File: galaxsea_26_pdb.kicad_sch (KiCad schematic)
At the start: 0 parts

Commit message: Fix annotations
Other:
- sheet 5V BDC renamed BDC Module
- removed sheet 12V BDC
- sheet BDC Module: file 5V_BDC_Module.kicad_sch -> BDC_Module.kicad_sch
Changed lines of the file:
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@@
 	(paper "A4")
 	(sheet
-		(at 174.625 53.34)
+		(at 198.755 33.655)
 		(size 53.975 34.925)
 		(exclude_from_sim no)
@@
 			(color 0 0 0 0.0000)
 		)
-		(property "Sheetname" "5V BDC"
-			(at 174.625 52.6284 0)
+		(property "Sheetname" "BDC Module"
+			(at 198.755 32.9434 0)
 			(effects
 				(font
@@
 			)
 		)
-		(property "Sheetfile" "5V_BDC_Module.kicad_sch"
-			(at 174.625 88.8496 0)
+		(property "Sheetfile" "BDC_Module.kicad_sch"
+			(at 198.755 69.1646 0)
 			(effects
 				(font
@@
 				)
 			)
-		)
-	)
-	(sheet
-		(at 175.26 99.06)
-		(size 53.975 34.925)
-		(exclude_from_sim no)
-		(in_bom yes)
-		(on_board yes)
-		(dnp no)
-		(fields_autoplaced yes)
-		(stroke
-			(width 0.1524)
-			(type solid)
-		)
-		(fill
-			(color 0 0 0 0.0000)
-		)
-		(property "Sheetname" "12V BDC"
-			(at 175.26 98.3484 0)
-			(effects
-				(font
-					(size 1.27 1.27)
-				)
-				(justify left bottom)
-			)
-		)
-		(property "Sheetfile" "12V_BDC_Module.kicad_sch"
-			(at 175.26 134.5696 0)
-			(effects
-				(font
-					(size 1.27 1.27)
-				)
-				(justify left top)
-			)
-		)
-		(instances
-			(project "galaxsea_26_pdb"
-				(path "/62a79688-1caa-411a-b477-96e92006e83c"
-					(page "3")
-				)
-			)

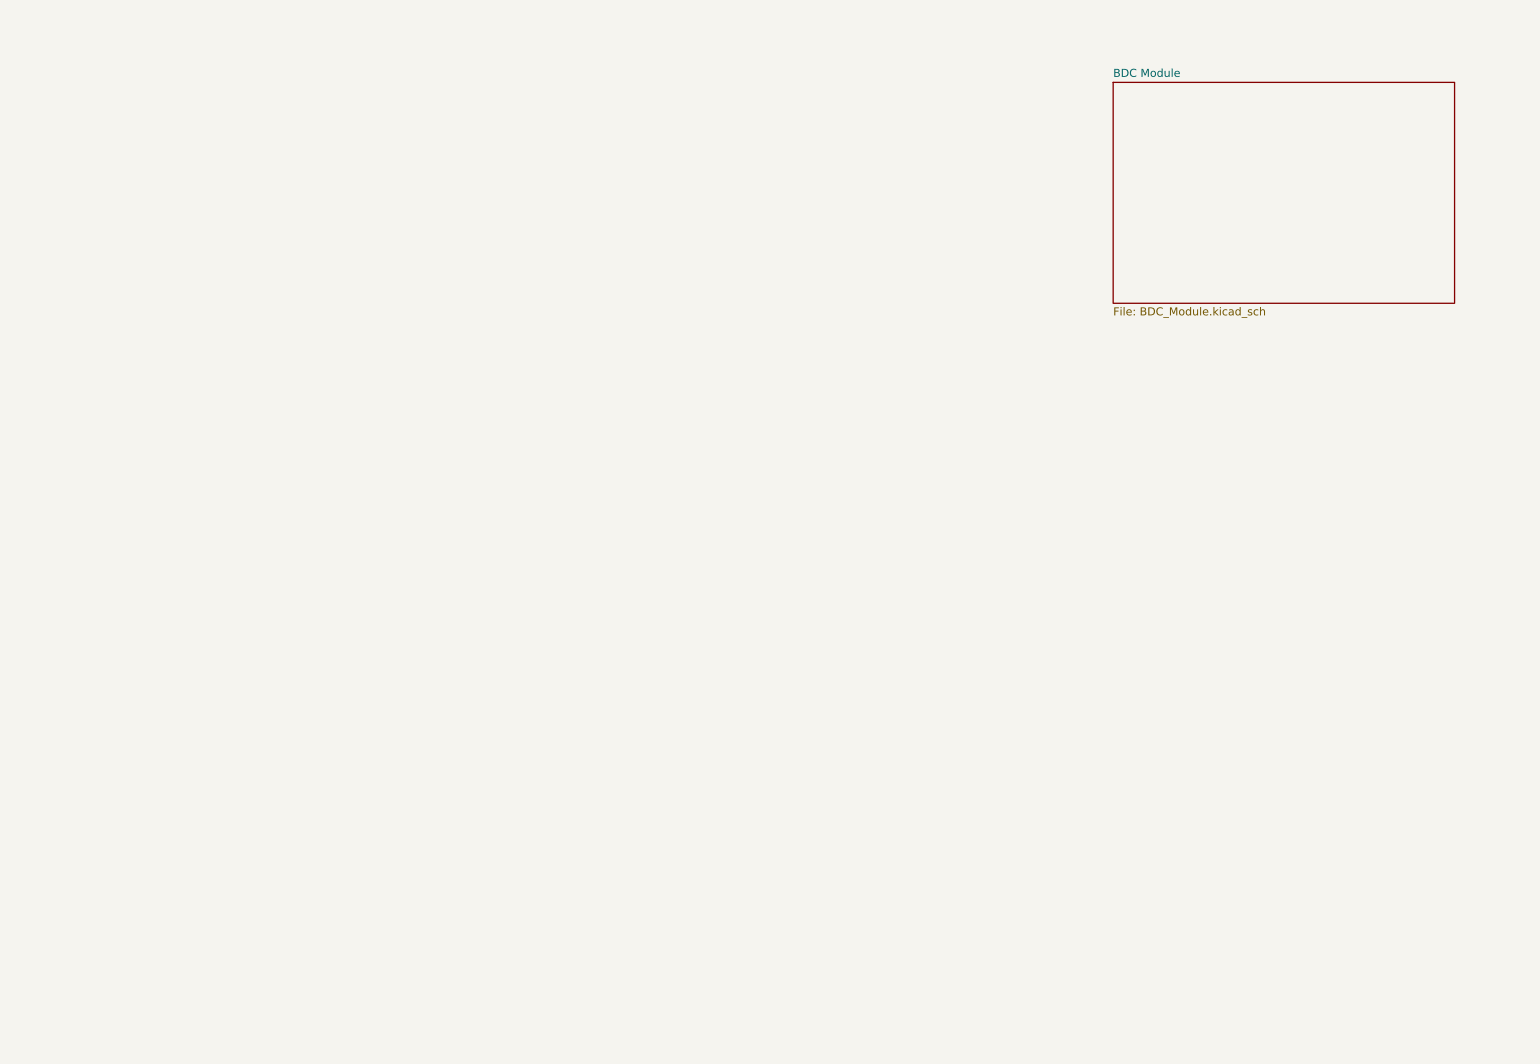
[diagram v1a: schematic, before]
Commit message: add JLCPCB design rules
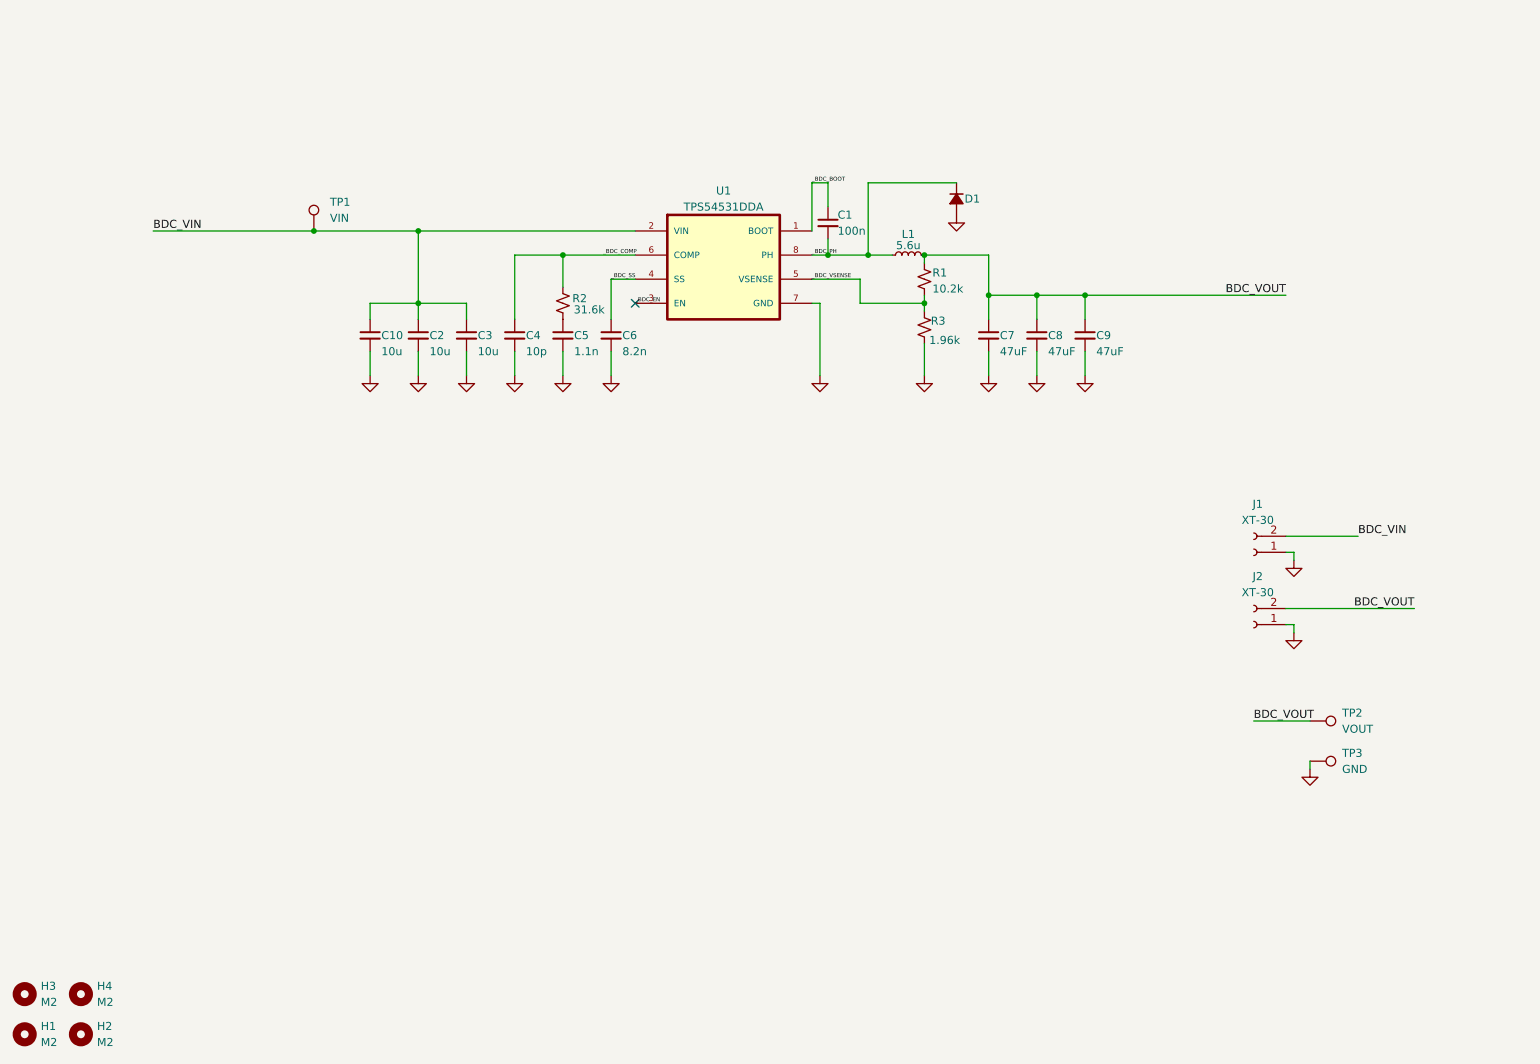
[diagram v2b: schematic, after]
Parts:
- added C1: 100n, Capacitor_SMD:C_0805_2012Metric, symbol Device:C_Small
- added C10, C2, C3: 10u, Capacitor_SMD:C_0805_2012Metric, symbol Device:C_Small
- added C4: 10p, Capacitor_SMD:C_0805_2012Metric, symbol Device:C_Small
- added C5: 1.1n, Capacitor_SMD:C_0805_2012Metric, symbol Device:C_Small
- added C6: 8.2n, Capacitor_SMD:C_0805_2012Metric, symbol Device:C_Small
- added C7, C8, C9: 47uF, Capacitor_SMD:C_0805_2012Metric, symbol Device:C_Small
- added D1: CHANGE FOOTPRINT LATER, Diode_SMD:D_SMC, symbol Device:D_Small_Filled
- added H1, H2, H3, H4: M2, MountingHole:MountingHole_2.2mm_M2, symbol Mechanical:MountingHole
- added J1, J2: XT-30, Connector_AMASS:AMASS_XT60-F_1x02_P7.20mm_Vertical, symbol Connector:Conn_01x02_Socket
- added L1: 5.6u, Inductor_SMD:L_Vishay_IHLP-2525, symbol Device:L_Small
- added R1: 10.2k, Resistor_SMD:R_0805_2012Metric, symbol Device:R_Small_US
- added R2: 31.6k, Resistor_SMD:R_0805_2012Metric, symbol Device:R_Small_US
- added R3: 1.96k, Resistor_SMD:R_0805_2012Metric, symbol Device:R_Small_US
- added TP1: VIN, TestPoint:TestPoint_Keystone_5005-5009_Compact, symbol Connector:TestPoint
- added TP2: VOUT, TestPoint:TestPoint_Keystone_5005-5009_Compact, symbol Connector:TestPoint
- added TP3: GND, TestPoint:TestPoint_Keystone_5005-5009_Compact, symbol Connector:TestPoint
- added U1: TPS54531DDA, footprints:VREG_LM5017MR_NOPB, symbol TPS54531DDA:TPS54531DDA
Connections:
- new net: C5.1, R2.1
- new net BDC_VIN: C10.1, C2.1, C3.1, J1.2 (Pin_2), TP1.1, U1.2 (VIN)
- new net BDC_VOUT: C7.1, C8.1, C9.1, J2.2 (Pin_2), L1.2, R1.1, TP2.1
- new net GND: C10.2, C2.2, C3.2, C4.2, C5.2, C6.2, C7.2, C8.2, C9.2, D1.2 (A), J1.1 (Pin_1), J2.1 (Pin_1), R3.2, TP3.1, U1.7 (GND)
- new net _BDC_BOOT: C1.1, U1.1 (BOOT)
- new net _BDC_COMP: C4.1, R2.2, U1.6 (COMP)
- new net _BDC_EN: U1.3 (EN)
- new net _BDC_PH: C1.2, D1.1 (K), L1.1, U1.8 (PH)
- new net _BDC_SS: C6.1, U1.4 (SS)
- new net _BDC_VSENSE: R1.2, R3.1, U1.5 (VSENSE)
- no-connect marks 0 -> 1
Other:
- removed sheet BDC Module

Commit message: move test and production modules into seperate hierarchical sheets
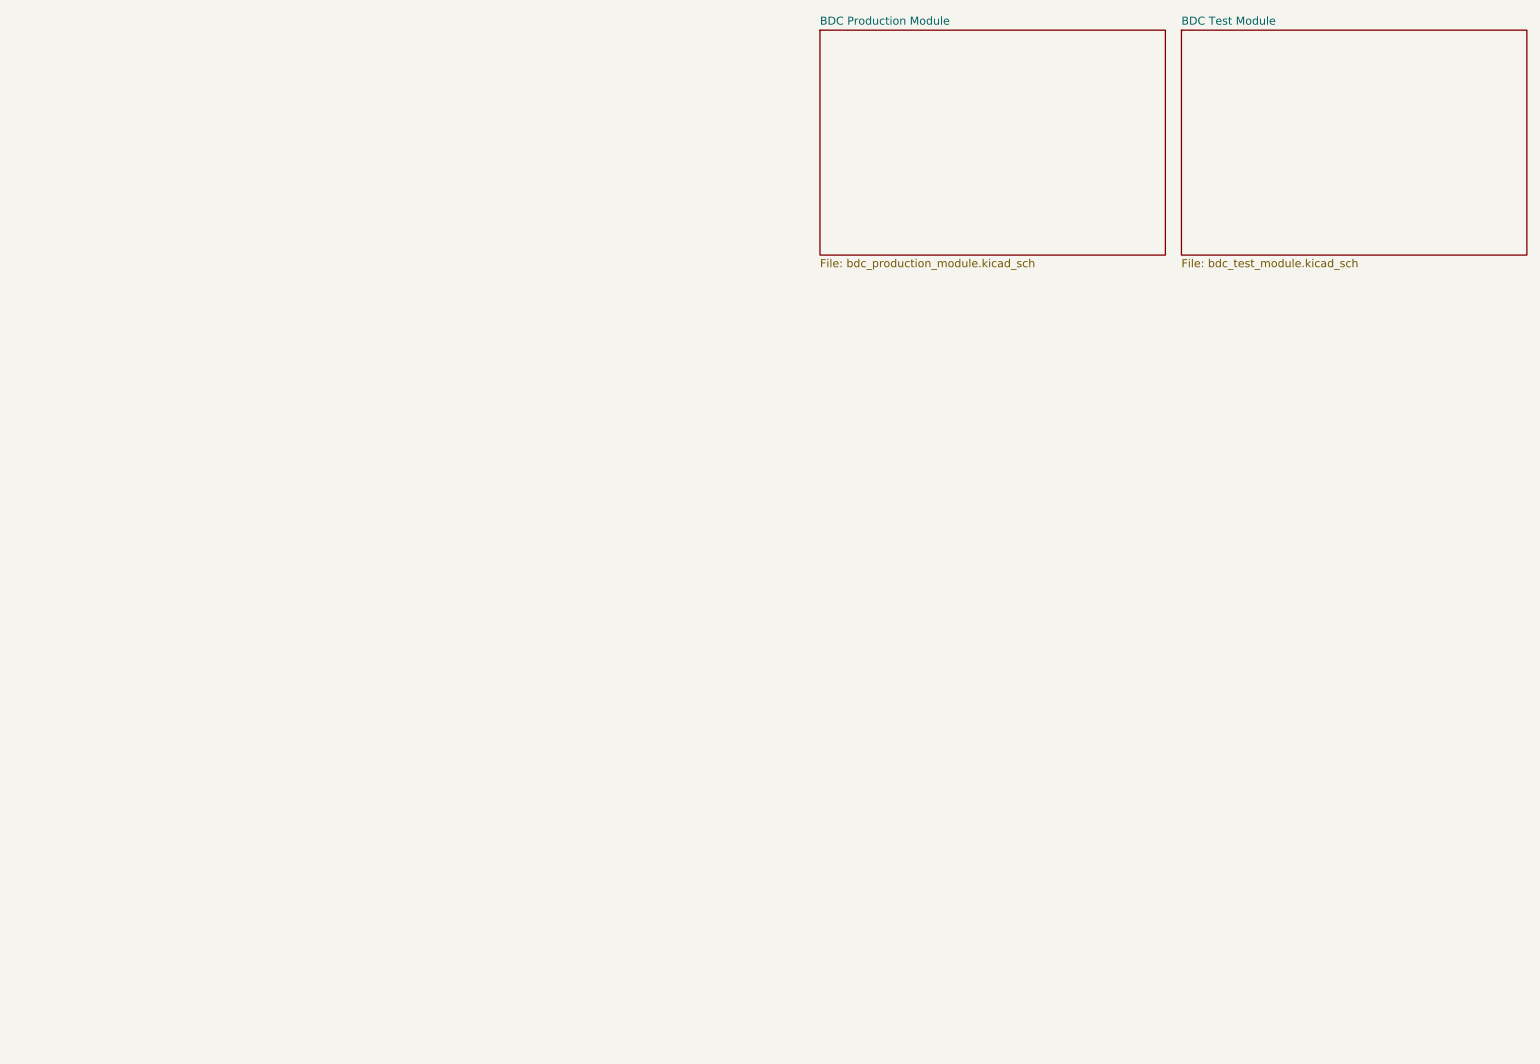
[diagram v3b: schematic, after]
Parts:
- removed C1: 100n, Capacitor_SMD:C_0805_2012Metric, symbol Device:C_Small
- removed C10, C2, C3: 10u, Capacitor_SMD:C_0805_2012Metric, symbol Device:C_Small
- removed C4: 10p, Capacitor_SMD:C_0805_2012Metric, symbol Device:C_Small
- removed C5: 1.1n, Capacitor_SMD:C_0805_2012Metric, symbol Device:C_Small
- removed C6: 8.2n, Capacitor_SMD:C_0805_2012Metric, symbol Device:C_Small
- removed C7, C8, C9: 47uF, Capacitor_SMD:C_0805_2012Metric, symbol Device:C_Small
- removed D1: CHANGE FOOTPRINT LATER, Diode_SMD:D_SMC, symbol Device:D_Small_Filled
- removed H1, H2, H3, H4: M2, MountingHole:MountingHole_2.2mm_M2, symbol Mechanical:MountingHole
- removed J1, J2: XT-30, Connector_AMASS:AMASS_XT60-F_1x02_P7.20mm_Vertical, symbol Connector:Conn_01x02_Socket
- removed L1: 5.6u, Inductor_SMD:L_Vishay_IHLP-2525, symbol Device:L_Small
- removed R1: 10.2k, Resistor_SMD:R_0805_2012Metric, symbol Device:R_Small_US
- removed R2: 31.6k, Resistor_SMD:R_0805_2012Metric, symbol Device:R_Small_US
- removed R3: 1.96k, Resistor_SMD:R_0805_2012Metric, symbol Device:R_Small_US
- removed TP1: VIN, TestPoint:TestPoint_Keystone_5005-5009_Compact, symbol Connector:TestPoint
- removed TP2: VOUT, TestPoint:TestPoint_Keystone_5005-5009_Compact, symbol Connector:TestPoint
- removed TP3: GND, TestPoint:TestPoint_Keystone_5005-5009_Compact, symbol Connector:TestPoint
- removed U1: TPS54531DDA, footprints:VREG_LM5017MR_NOPB, symbol TPS54531DDA:TPS54531DDA
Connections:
- no-connect marks 1 -> 0
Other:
- added sheet BDC Production Module (bdc_production_module.kicad_sch)
- added sheet BDC Test Module (bdc_test_module.kicad_sch)

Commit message: Initial PDB layout
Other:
- added sheet PDB (pdb.kicad_sch)
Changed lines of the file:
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@@
+	)
+	(sheet
+		(at 95.25 25.4)
+		(size 54.61 35.56)
+		(exclude_from_sim no)
+		(in_bom yes)
+		(on_board yes)
+		(dnp no)
+		(fields_autoplaced yes)
+		(stroke
+			(width 0.1524)
+			(type solid)
+		)
+		(fill
+			(color 0 0 0 0.0000)
+		)
+		(property "Sheetname" "PDB"
+			(at 95.25 24.6884 0)
+			(effects
+				(font
+					(size 1.27 1.27)
+				)
+				(justify left bottom)
+			)
+		)
+		(property "Sheetfile" "pdb.kicad_sch"
+			(at 95.25 61.5446 0)
+			(effects
+				(font
+					(size 1.27 1.27)
+				)
+				(justify left top)
+			)
+		)
+		(instances
+			(project "galaxsea_26_pdb"
+				(path "/62a79688-1caa-411a-b477-96e92006e83c"
+					(page "4")
+				)
+			)
+		)
 	)
 	(sheet
